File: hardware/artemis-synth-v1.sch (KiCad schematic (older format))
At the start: 55 parts, among them IC1 ATMEGA328P, J1 USB_2, J2 AVR-ISP-6, SW10 SWITCH_PUSH_CW, SW11 SWITCH_PUSH_CW, SW2 SWITCH_PUSH_CW, SW3 SWITCH_PUSH_CW, SW4 SWITCH_PUSH_CW, SW5 SWITCH_PUSH_CW, SW6 SWITCH_PUSH_CW, SW7 SWITCH_PUSH_CW, SW8 SWITCH_PUSH_CW, SW9 SWITCH_PUSH_CW, U1 MCP4921, U2 TDA2822M, X1 16MHz

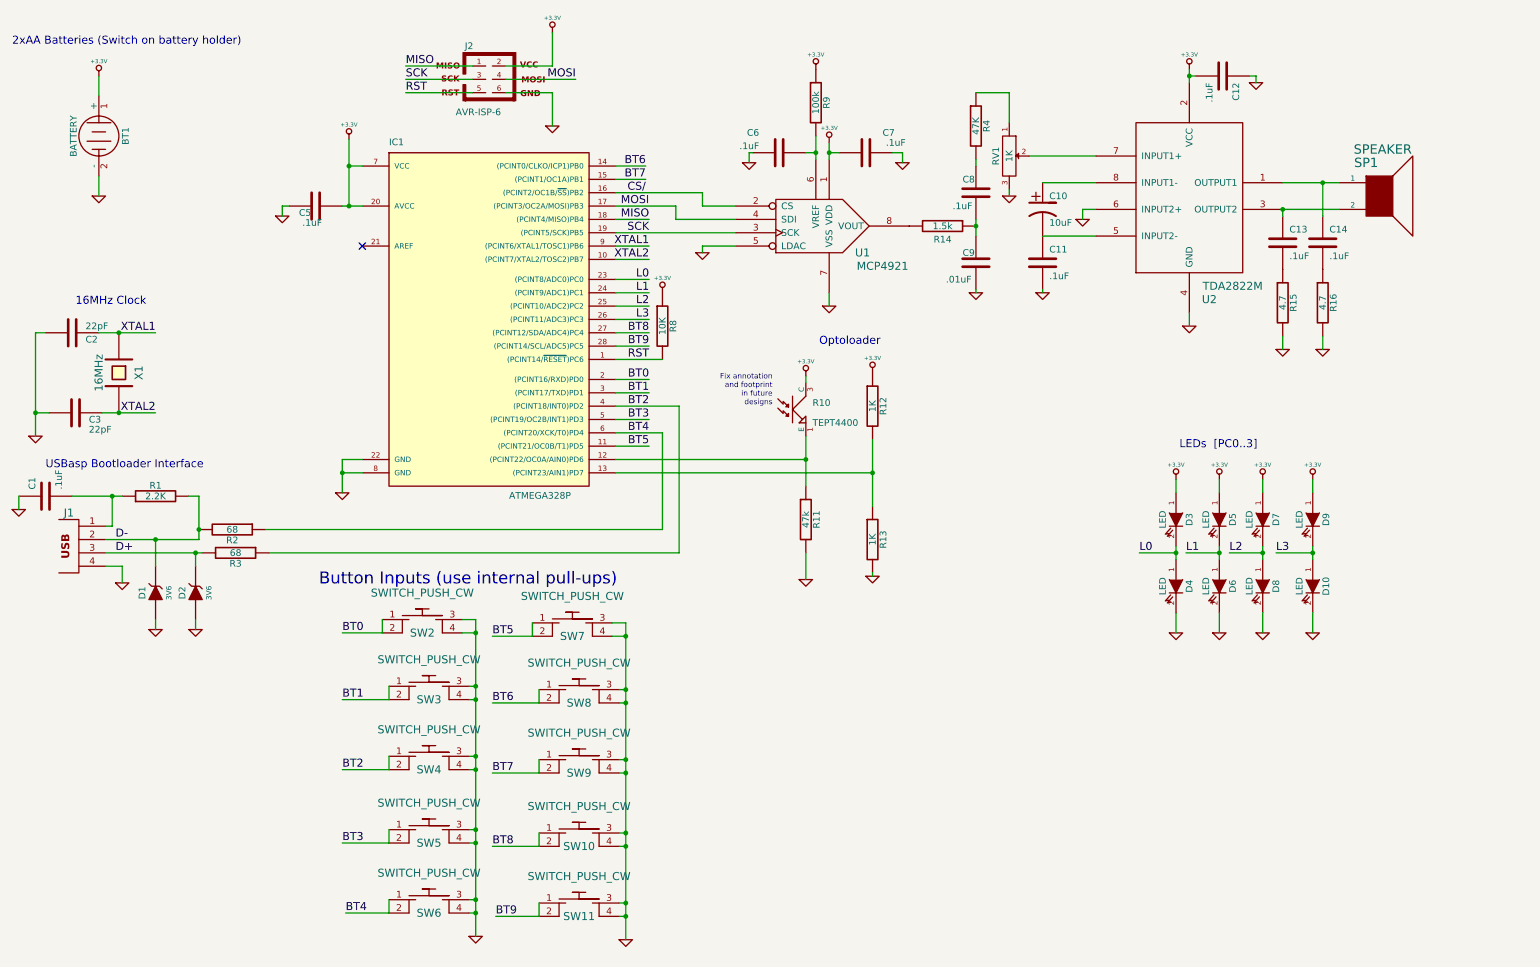
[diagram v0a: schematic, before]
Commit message: Took out USB interface. Added power indication LED. Removed external xtal. Removed speaker. Removed output interface. Added line level output and audio jack. All changes are to schematic. PCB layout has not been updated.
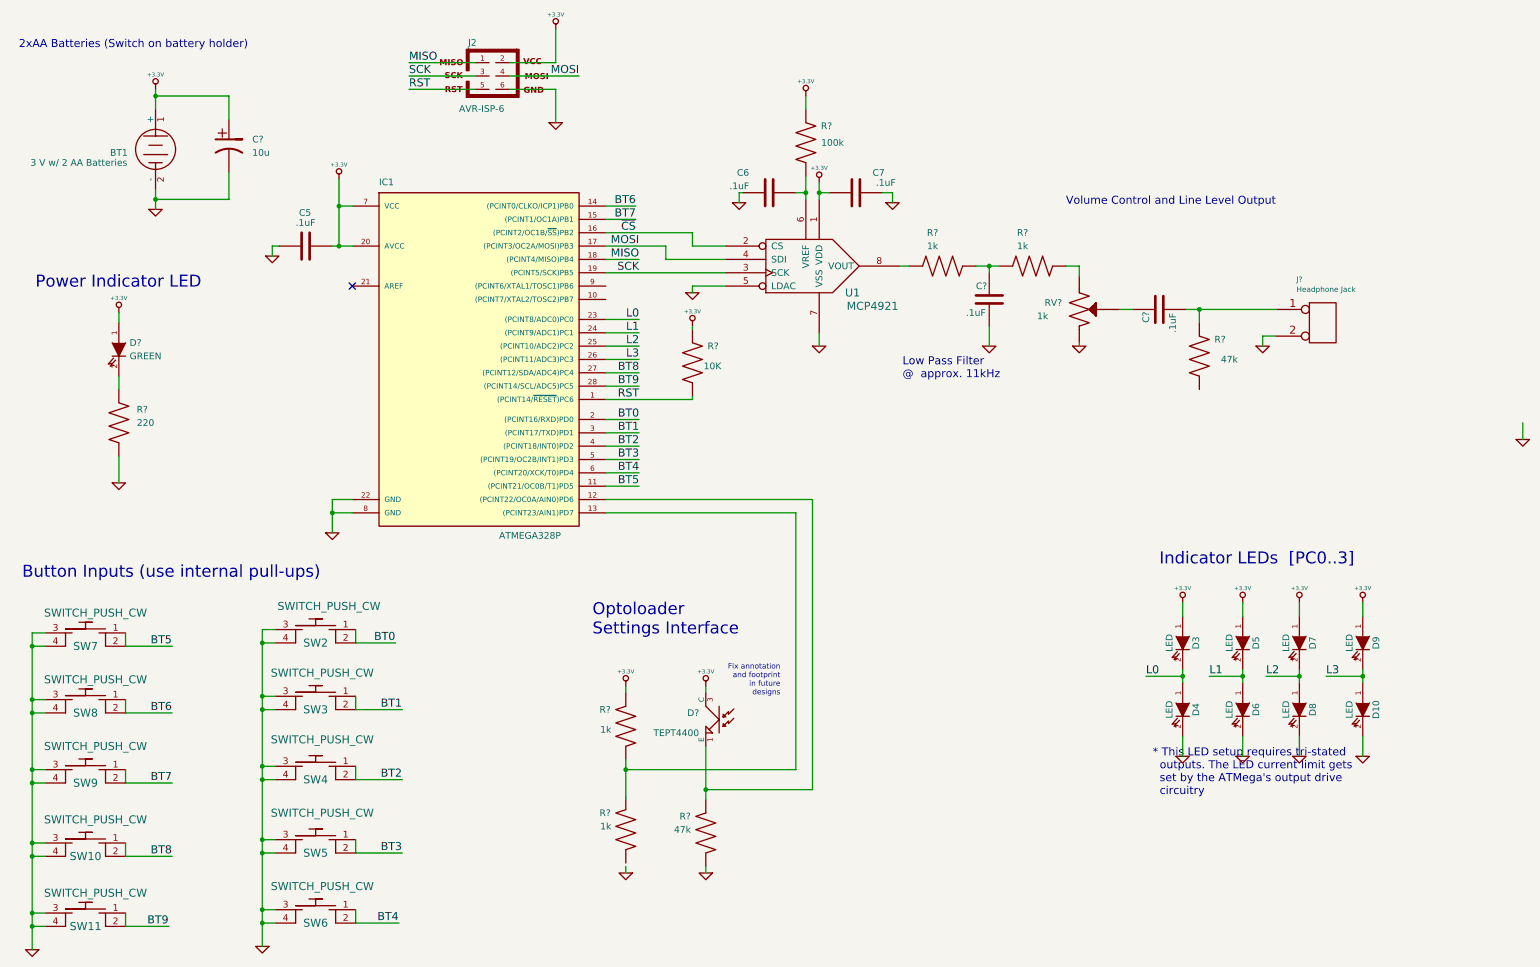
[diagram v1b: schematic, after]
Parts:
- removed C1, C11, C12, C13, C14, C8: .1uF, C1, symbol C
- removed C10: 10uF, SparkFun-CPOL-RADIAL-10UF-25V, symbol CP1
- removed C2, C3: 22pF, C1, symbol C
- removed C9: .01uF, C1, symbol C
- removed D1, D2: 3V6, D4, symbol ZENER
- removed J1: USB_2, USB_B, symbol USB_2
- removed R1: 2.2K, R4, symbol R
- removed R11: 47k, R4, symbol R
- removed R12, R13: 1K, R4, symbol R
- removed R14: 1.5k, R4, symbol R
- removed R15, R16: 4.7, R4, symbol R
- removed R2, R3: 68, R4, symbol R
- removed R4: 47K, R4, symbol R
- removed R8: 10K, R4, symbol R
- removed R9: 100k, R4, symbol R
- removed RV1: 1K, THUMBWHEEL_POT_3352T, symbol POT
- removed SP1: SPEAKER, 2PIN, symbol SPEAKER
- removed U2: TDA2822M, DIP-8__300, symbol TDA2822M
- removed X1: 16MHz, HC-49V, symbol CRYSTAL
- added C? (x2): .1uF, C1, symbol C
- added C?: 10u, symbol CP1
- added D?: GREEN, symbol LED
- added J?: Headphone Jack, symbol CONN_2
- added R? (x4): 1k, symbol R_US
- added R? (x2): 47k, symbol R_US
- added R?: 100k, symbol R_US
- added R?: 10K, symbol R_US
- added R?: 220, symbol R_US
- added RV?: 1k, symbol POT_US
- BT1: value BATTERY -> 3 V w/ 2 AA Batteries
- renumbered R10 to D?
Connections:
- net labels added: ~CS
- net labels removed: CS/, D+, D-, XTAL1, XTAL2
- wire segments 167 -> 179
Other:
- note added: "* This LED setup requires tri-stated\n outputs. The LED current limit gets\n set by the ATMega's output drive\n circuitry"
- note added: "Indicator LEDs [PC0..3]"
- note added: "Low Pass Filter \n@ approx. 11kHz\n"
- note added: "Optoloader\nSettings Interface"
- note added: "Power Indicator LED"
- note added: "Volume Control and Line Level Output"
- note removed: "16MHz Clock"
- note removed: "LEDs [PC0..3]"
- note removed: "Optoloader\n"
- note removed: "USBasp Bootloader Interface\n"
- moved on the sheet: BT1, C5, C6, C7, D10, D3, D4, D5, D6, D7, D8, D9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

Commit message: made a pcb layout for the enw design. It is the same size, but has different text a few different headers and overall less parts.
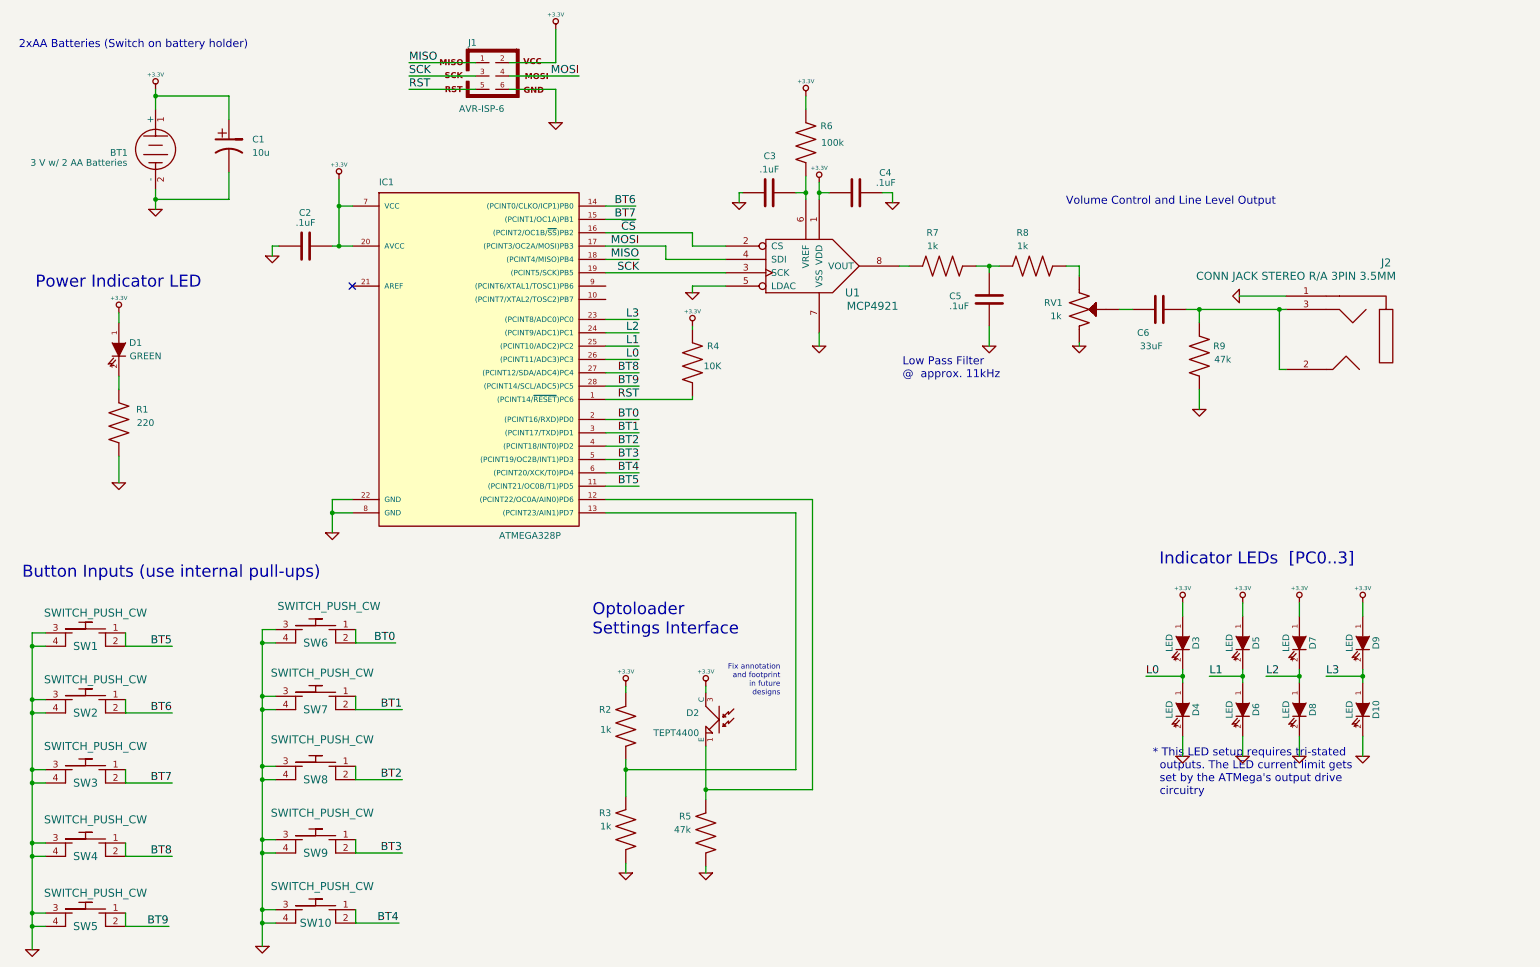
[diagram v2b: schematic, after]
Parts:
- removed J?: Headphone Jack, symbol CONN_2
- added J2: CONN JACK STEREO R/A 3PIN 3.5MM, symbol 3-PIN_AUDIO_JACK
- C6: renamed from C?; value .1uF -> 33uF
- gave numbers to parts that had none: 14
- renumbered C5 to C2, C6 to C3, C7 to C4, J2 to J1, SW7 to SW1, SW6 to SW10, SW8 to SW2, SW9 to SW3, SW10 to SW4, SW11 to SW5, SW2 to SW6, SW3 to SW7, SW4 to SW8, SW5 to SW9
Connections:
- wire segments 179 -> 147
